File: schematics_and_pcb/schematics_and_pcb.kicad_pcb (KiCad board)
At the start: 2 copper layers, 51.1 x 89.8 mm, 68 parts, among them J1 RND 205-00624, J2 RND 205-00627, J3 Motor con, J4 Conn_01x04_Male, J5 Conn_01x04_Male, J6 USB_OTG_custom, Q1 TSM2308CX RFG, SW1 RND 210-00210, SW2 SW_Push, U1 LP2985IM5-2.0/NOPB, U2 TS3480CX33 RFG, U3 PWM3389DM-T3QU, U4 STM32F401RBTx, U5 LFXTAL055951

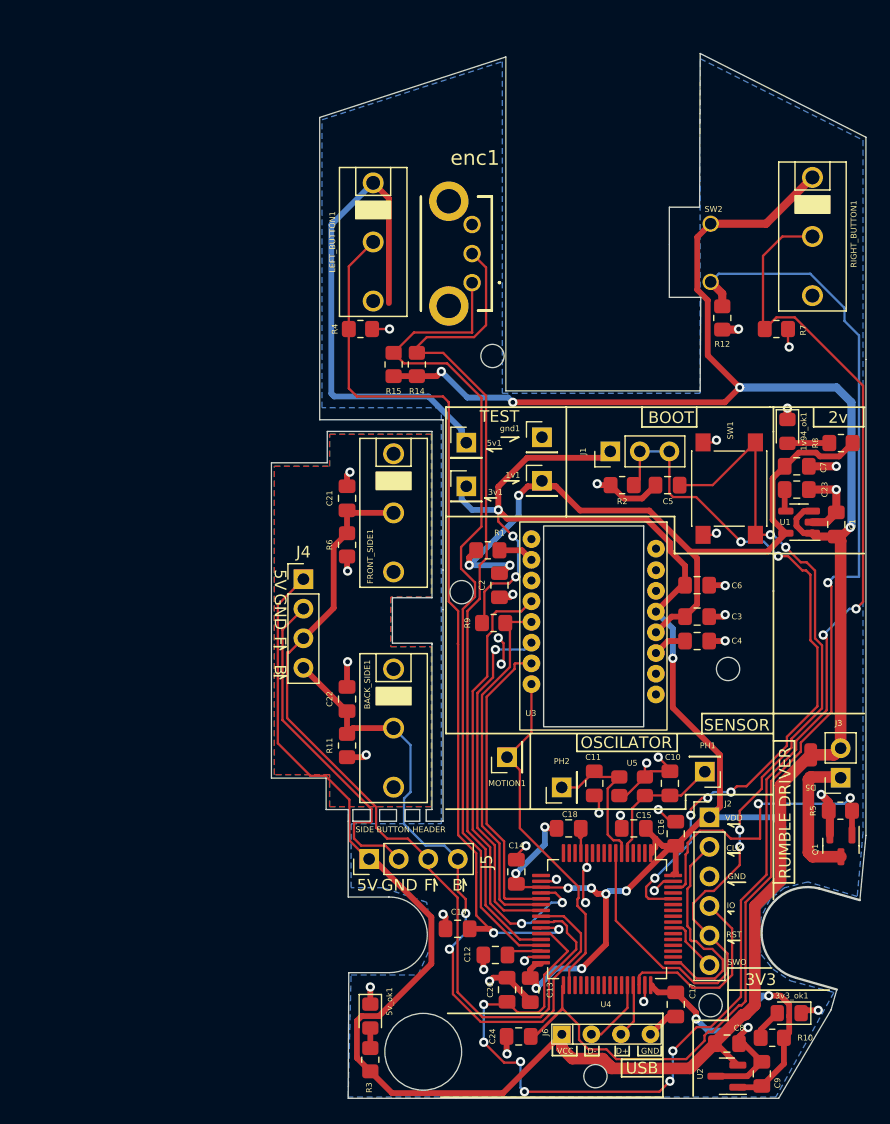
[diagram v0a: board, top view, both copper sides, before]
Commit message: added RGB LEDS
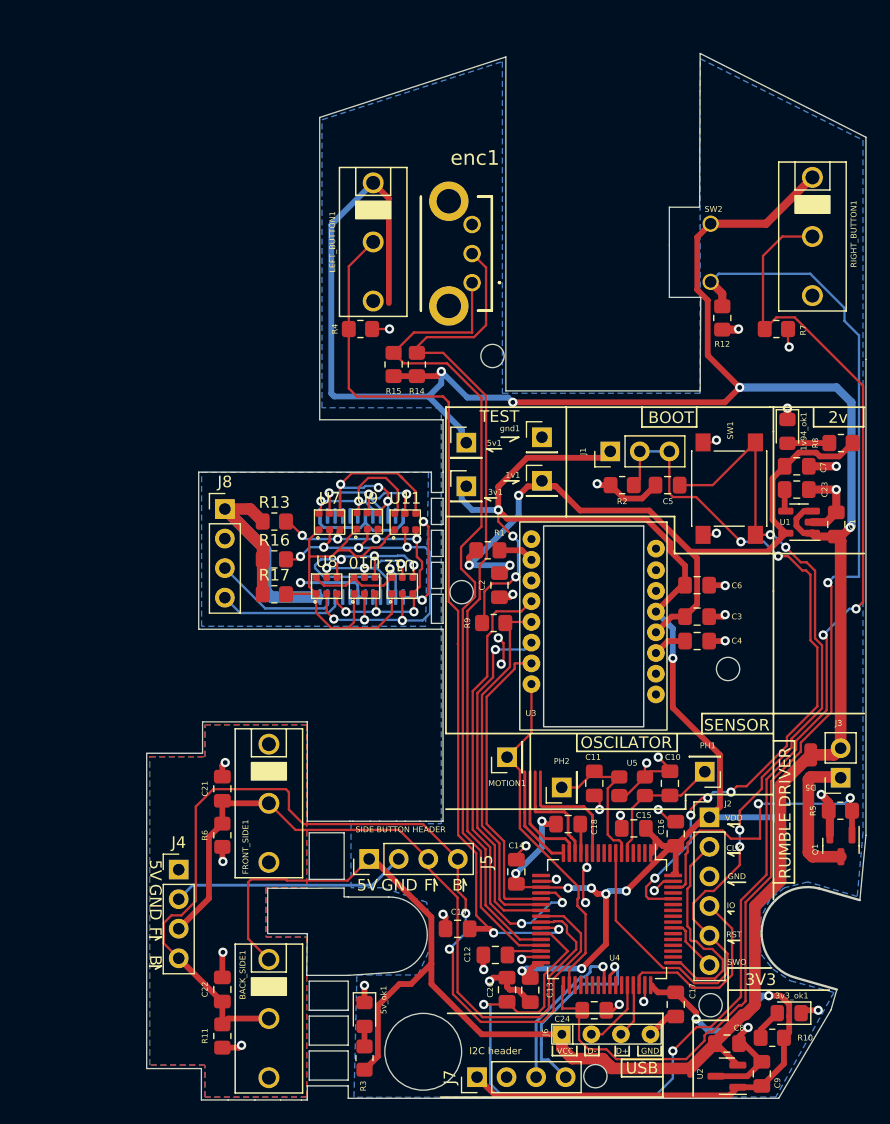
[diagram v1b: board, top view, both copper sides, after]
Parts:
- added J7: i2c header, Connector_PinHeader_2.54mm:PinHeader_1x04_P2.54mm_Vertical, F.Cu at (96.9, 112.5)
- added J8: i2c header, Connector_PinHeader_2.54mm:PinHeader_1x04_P2.54mm_Vertical, F.Cu at (75.2, 63.7)
- added R13: 680m, Resistor_SMD:R_0805_2012Metric_Pad1.20x1.40mm_HandSolder, F.Cu at (79.5, 64.8)
- added R16: 680m, Resistor_SMD:R_0805_2012Metric_Pad1.20x1.40mm_HandSolder, F.Cu at (79.5, 68.0)
- added R17: 8.2, Resistor_SMD:R_0805_2012Metric_Pad1.20x1.40mm_HandSolder, F.Cu at (79.5, 71.0)
- added U10: RND 135-00249, mouse:RND_135-00249, F.Cu at (87.2, 70.2)
- added U11: RND 135-00249, mouse:RND_135-00249, F.Cu at (90.8, 64.8)
- added U12: RND 135-00249, mouse:RND_135-00249, F.Cu at (90.5, 70.2)
- added U6: 9DB403DGLFT, mouse:TSSOP-24, B.Cu at (83.4, 64.3)
- added U7: RND 135-00249, mouse:RND_135-00249, F.Cu at (84.2, 64.8)
- added U8: RND 135-00249, mouse:RND_135-00249, F.Cu at (84.0, 70.2)
- added U9: RND 135-00249, mouse:RND_135-00249, F.Cu at (87.5, 64.7)
- moved BACK_SIDE1 27.2 mm to (79.0, 107.5)
- moved C21 27.2 mm to (75.0, 87.7)
- moved C22 27.2 mm to (75.0, 105.0)
- moved FRONT_SIDE1 27.2 mm to (79.0, 89.0)
- moved R11 27.2 mm to (75.0, 109.0)
- moved R6 27.2 mm to (75.0, 91.7)
- moved J4 27.2 mm to (71.3, 94.7)
- moved C24 6.88 mm to (107.0, 106.8), turned to 180 degrees
- moved 5v_ok1 0.52 mm to (87.2, 107.1)
- moved R3 0.52 mm to (87.2, 110.9)
- moved C18 0.37 mm to (104.8, 90.8)
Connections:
- U4 pad 40: MCO2 -> SDA
- U4 pad 41: MCO1 -> SCL
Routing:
- net VDDIO: track 171.5 -> 222.6 mm
- net VDDG: track 0.00 -> 39.0 mm, vias 0 -> 7
- net VDDR: track 0.00 -> 34.2 mm
- net VDDB: track 0.00 -> 30.6 mm, vias 0 -> 7
- net SCL: track 0.00 -> 28.4 mm, vias 0 -> 1
- net BACK_STATE: track 60.7 -> 87.5 mm
- net SDA: track 0.00 -> 25.4 mm, vias 0 -> 1
- net PWM6: track 0.00 -> 21.7 mm, vias 0 -> 3
- net PWM2: track 0.00 -> 20.0 mm, vias 0 -> 3
- net GND: track 119.4 -> 135.6 mm, vias 39 -> 42
- net PWM0: track 0.00 -> 14.9 mm, vias 0 -> 2
- net PWM1: track 0.00 -> 14.5 mm, vias 0 -> 3
- net PWM5: track 0.00 -> 13.5 mm, vias 0 -> 3
- net +5V: track 273.2 -> 260.3 mm
- net PWM4: track 0.00 -> 11.7 mm, vias 0 -> 1
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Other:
- board size 51.1 x 89.8 mm -> 61.8 x 89.9 mm
- board text added: "I2C header"
- board text added: "SCL"
- board text added: "SDA"
- board text added: "VDDIO"

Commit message: some patches
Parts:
- moved J8 1.75 mm to (73.5, 63.7)
- moved R13 1.75 mm to (77.8, 64.8)
- moved R16 1.75 mm to (77.8, 68.0)
- moved R17 1.75 mm to (77.8, 71.0)
- moved U10 1.75 mm to (85.5, 70.2)
- moved U11 1.75 mm to (89.0, 64.8)
- moved U12 1.75 mm to (88.8, 70.2)
- moved U6 1.75 mm to (81.7, 64.3)
- moved U7 1.75 mm to (82.5, 64.8)
- moved U8 1.75 mm to (82.2, 70.2)
- moved U9 1.75 mm to (85.8, 64.7)
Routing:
- net BACK_STATE: track 87.5 -> 45.7 mm
- net GND: track 135.6 -> 115.2 mm
- net +5V: track 260.3 -> 241.5 mm
- net FRONT_STATE: track 64.7 -> 49.0 mm
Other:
- outline, holes or cut-outs redrawn

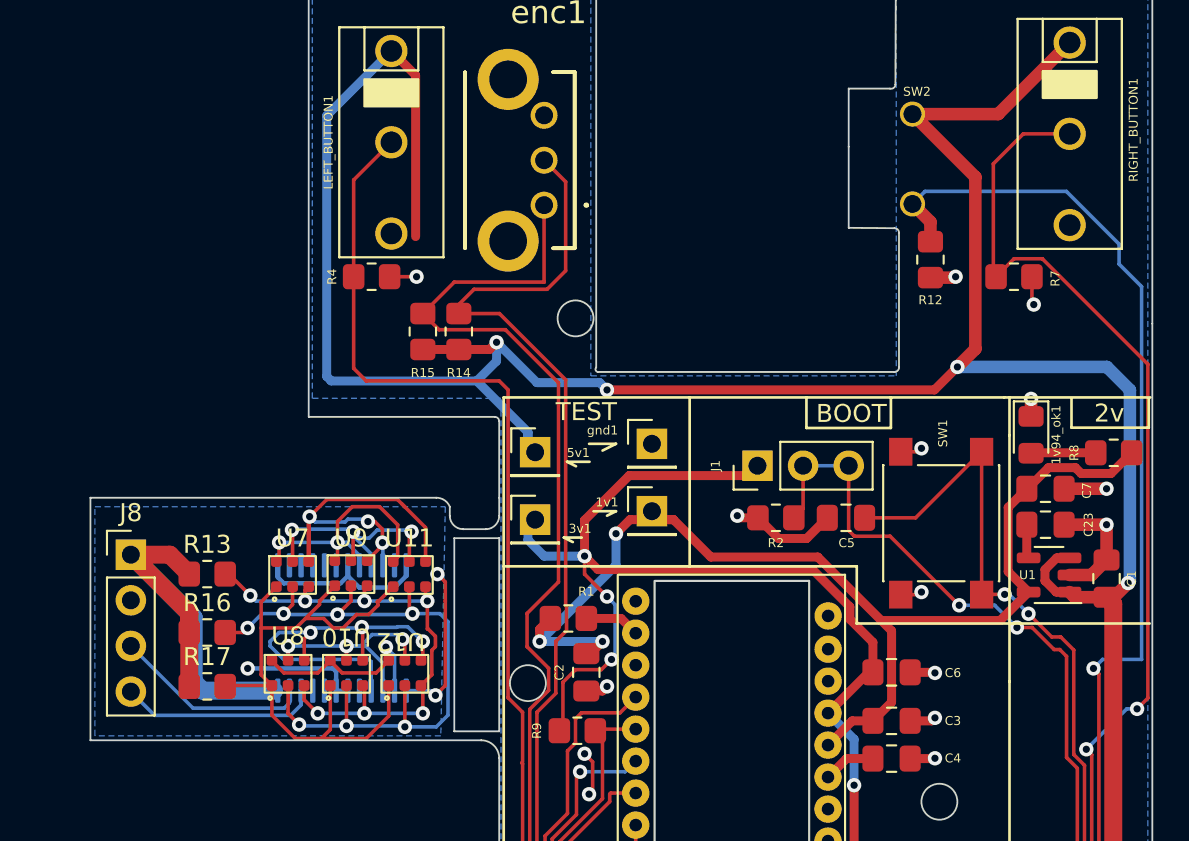
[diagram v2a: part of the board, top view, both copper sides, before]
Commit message: added pullups
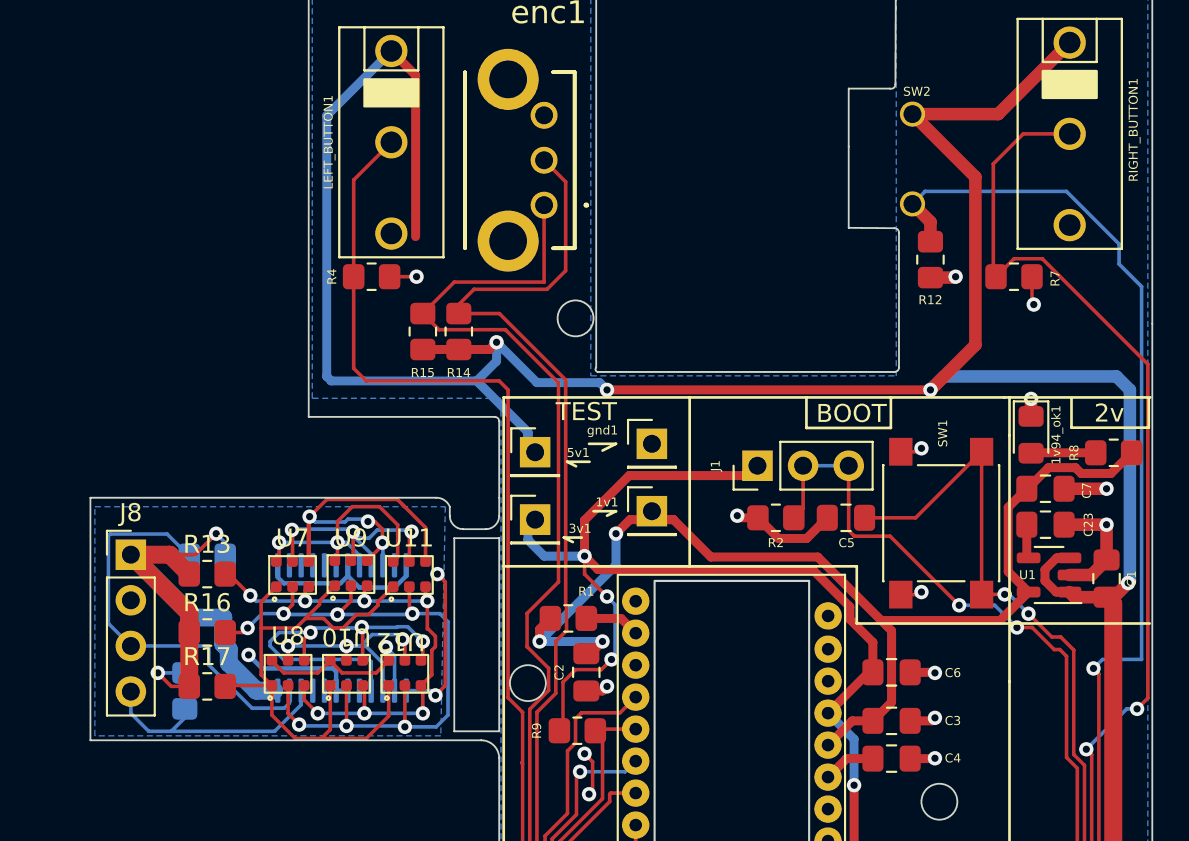
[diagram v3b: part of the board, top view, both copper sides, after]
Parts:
- added R18: 10k, Resistor_SMD:R_0805_2012Metric_Pad1.20x1.40mm_HandSolder, B.Cu at (76.5, 71.2)
- added R19: 10k, Resistor_SMD:R_0805_2012Metric_Pad1.20x1.40mm_HandSolder, B.Cu at (77.8, 63.8)
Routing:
- net SDA: track 25.4 -> 37.7 mm
- net VDDIO: track 222.6 -> 232.1 mm, vias 14 -> 16
- net SCL: track 28.4 -> 31.4 mm
- net +5V: track 241.5 -> 243.0 mm

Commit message: done with the bom
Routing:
- net unconnected-(U4-Pad11): track 11.0 -> 0.00 mm
- net unconnected-(U4-Pad14): track 9.88 -> 0.00 mm
- net unconnected-(U4-Pad15): track 9.42 -> 0.00 mm
- net unconnected-(U4-Pad16): track 8.96 -> 0.00 mm
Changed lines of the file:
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@@
   (gr_line (start 75 66.5) (end 75.75 66.75) (layer "B.SilkS") (width 0.15))
   (gr_line (start 75 64.5) (end 75.75 64.75) (layer "B.SilkS") (width 0.15))
-  (gr_line (start 75 72.25) (end 75.75 72.5) (layer "B.SilkS") (width 0.15))
   (gr_line (start 76.75 69.5) (end 75 69.5) (layer "B.SilkS") (width 0.15))
-  (gr_line (start 77 72.25) (end 75 72.25) (layer "B.SilkS") (width 0.15))
   (gr_line (start 75 69.5) (end 75.75 69.75) (layer "B.SilkS") (width 0.15))
   (gr_line (start 77.75 64.5) (end 75 64.5) (layer "B.SilkS") (width 0.15))
@@
   (gr_line (start 73.2375 112.5) (end 73.2325 114.4625) (layer "Edge.Cuts") (width 0.1))
   (gr_line (start 116.25 53.25) (end 116.25 45.75) (layer "Edge.Cuts") (width 0.1))
-  (gr_arc (start 99.5 53.5) (mid 99.369135 53.407575) (end 99.39808 53.25) (layer "Edge.Cuts") (width 0.1))
+  (gr_arc (start 99.5 53.5) (mid 99.369135 53.407576) (end 99.39808 53.25) (layer "Edge.Cuts") (width 0.1))
   (gr_line (start 83.39808 56) (end 83.39808 30.018068) (layer "Edge.Cuts") (width 0.1))
   (gr_line (start 92 90.5) (end 92.55 90.5) (layer "Edge.Cuts") (width 0.1))
@@
     (effects (font (size 0.75 0.75) (thickness 0.15)) (justify mirror))
   )
-  (gr_text "SCL\n" (at 76 71.5) (layer "B.SilkS")
+  (gr_text "SCL\n" (at 73.5 73.25) (layer "B.SilkS")
     (effects (font (size 0.75 0.75) (thickness 0.15)) (justify mirror))
   )
@@
   (segment (start 101.006148 75.75) (end 101.59808 75.158068) (width 0.2) (layer "B.Cu") (net 25))
   (segment (start 98.5 75.75) (end 101.006148 75.75) (width 0.2) (layer "B.Cu") (net 25))
-  (segment (start 104.45048 89.70048) (end 103.25 89.70048) (width 0.25) (layer "F.Cu") (net 26))
-  (segment (start 105.34808 93.243068) (end 105.34808 92.212363) (width 0.25) (layer "F.Cu") (net 26))
-  (segment (start 105.034277 91.89856) (end 104.75 91.614283) (width 0.25) (layer "F.Cu") (net 26))
-  (segment (start 101.92404 89.67404) (end 101.92404 89.25) (width 0.25) (layer "F.Cu") (net 26))
-  (segment (start 105.34808 92.212363) (end 105.034277 91.89856) (width 0.25) (layer "F.Cu") (net 26))
-  (segment (start 104.75 91.614283) (end 104.75 90) (width 0.25) (layer "F.Cu") (net 26))
-  (segment (start 101.92404 89.25) (end 101.92404 86.25) (width 0.25) (layer "F.Cu") (net 26))
-  (segment (start 104.75 90) (end 104.45048 89.70048) (width 0.25) (layer "F.Cu") (net 26))
-  (segment (start 103.25 89.70048) (end 101.95048 89.70048) (width 0.25) (layer "F.Cu") (net 26))
-  (segment (start 101.95048 89.70048) (end 101.92404 89.67404) (width 0.25) (layer "F.Cu") (net 26))
   (segment (start 100.14952 76.993554) (end 100.149519 77.415487) (width 0.2) (layer "F.Cu") (net 27))
   (segment (start 101.59808 76.938068) (end 100.205006 76.938068) (width 0.2) (layer "F.Cu") (net 27))
@@
   (segment (start 105.84808 90.81058) (end 105.7875 90.75) (width 0.25) (layer "F.Cu") (net 56))
   (segment (start 105.84808 93.243068) (end 105.84808 90.81058) (width 0.25) (layer "F.Cu") (net 56))
-  (segment (start 106.09808 89.25) (end 102.5 89.25) (width 0.25) (layer "F.Cu") (net 64))
-  (segment (start 102.5 89.25) (end 102.37356 89.12356) (width 0.25) (layer "F.Cu") (net 64))
-  (segment (start 102.37356 89.12356) (end 102.37356 86.25) (width 0.25) (layer "F.Cu") (net 64))
-  (segment (start 106.84808 90) (end 106.09808 89.25) (width 0.25) (layer "F.Cu") (net 64))
-  (segment (start 106.84808 93.243068) (end 106.84808 90) (width 0.25) (layer "F.Cu") (net 64))
-  (segment (start 101.47452 90.73844) (end 101.47452 86.25) (width 0.25) (layer "F.Cu") (net 65))
-  (segment (start 104.84808 92.34808) (end 104.5 92) (width 0.25) (layer "F.Cu") (net 65))
-  (segment (start 104.5 92) (end 102.73608 92) (width 0.25) (layer "F.Cu") (net 65))
-  (segment (start 104.84808 93.243068) (end 104.84808 92.34808) (width 0.25) (layer "F.Cu") (net 65))
-  (segment (start 102.73608 92) (end 101.47452 90.73844) (width 0.25) (layer "F.Cu") (net 65))
-  (segment (start 102.100362 92) (end 101.025 90.924638) (width 0.25) (layer "F.Cu") (net 66))
-  (segment (start 101.025 90.924638) (end 101.025 89.75) (width 0.25) (layer "F.Cu") (net 66))
-  (segment (start 103.34343 93.243068) (end 102.100362 92) (width 0.25) (layer "F.Cu") (net 66))
-  (segment (start 101.025 89.75) (end 101.025 86.25) (width 0.25) (layer "F.Cu") (net 66))
-  (segment (start 104.34808 93.243068) (end 103.34343 93.243068) (width 0.25) (layer "F.Cu") (net 66))
   (segment (start 106.5 110.107968) (end 108.046768 110.107968) (width 0.2) (layer "F.Cu") (net 68))
   (segment (start 122.20048 87.068828) (end 124.75048 84.518828) (width 0.2) (layer "F.Cu") (net 68))

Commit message: updated the bom
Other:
- outline, holes or cut-outs redrawn
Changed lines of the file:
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@@
   (gr_line (start 118.49808 105.018068) (end 118.49808 107.618068) (layer "F.SilkS") (width 0.15))
   (gr_line (start 113.45 40.961932) (end 113.45 45.48) (layer "Edge.Cuts") (width 0.1))
-  (gr_line (start 90.75 90.5) (end 92 90.5) (layer "Edge.Cuts") (width 0.1))
   (gr_line (start 113.45 37.73) (end 113.45 40.961932) (layer "Edge.Cuts") (width 0.1))
-  (gr_line (start 86 90.5) (end 86.25 90.5) (layer "Edge.Cuts") (width 0.1))
   (gr_line (start 127.84808 104.968068) (end 124.34808 103.968068) (layer "Edge.Cuts") (width 0.2))
   (gr_arc (start 84.75 96.25) (mid 85.375 96.458333) (end 85.75 97) (layer "Edge.Cuts") (width 0.1))
   (gr_arc (start 80.25 100.1625) (mid 79.256047 99.768909) (end 78.9325 98.75) (layer "Edge.Cuts") (width 0.1))
-  (gr_line (start 83.5 90.5) (end 86 90.5) (layer "Edge.Cuts") (width 0.1))
-  (gr_line (start 88.55 90.5) (end 90 90.5) (layer "Edge.Cuts") (width 0.1))
+  (gr_line (start 83.75 90.7) (end 86.25 90.7) (layer "Edge.Cuts") (width 0.1))
   (gr_arc (start 90.5 60.5) (mid 90.950694 60.636459) (end 91.25 61) (layer "Edge.Cuts") (width 0.1))
   (gr_line (start 85.84808 103.75) (end 83 103.75) (layer "Edge.Cuts") (width 0.1))
@@
   (gr_line (start 122.84808 114.318068) (end 127.34808 106.718068) (layer "Edge.Cuts") (width 0.1))
   (gr_line (start 82.3325 114.4625) (end 81.8325 114.4625) (layer "Edge.Cuts") (width 0.1))
-  (gr_arc (start 93.75 56) (mid 93.926777 56.073223) (end 94 56.25) (layer "Edge.Cuts") (width 0.1))
+  (gr_arc (start 93.75 55.75) (mid 93.934017 55.970491) (end 94 56.25) (layer "Edge.Cuts") (width 0.1))
   (gr_line (start 99.39808 24.818068) (end 83.39808 30.018068) (layer "Edge.Cuts") (width 0.1))
   (gr_line (start 95.14808 114.318068) (end 122.84808 114.318068) (layer "Edge.Cuts") (width 0.1))
@@
   (gr_line (start 116.25 53.25) (end 116.25 45.75) (layer "Edge.Cuts") (width 0.1))
   (gr_arc (start 99.5 53.5) (mid 99.369135 53.407576) (end 99.39808 53.25) (layer "Edge.Cuts") (width 0.1))
-  (gr_line (start 83.39808 56) (end 83.39808 30.018068) (layer "Edge.Cuts") (width 0.1))
-  (gr_line (start 92 90.5) (end 92.55 90.5) (layer "Edge.Cuts") (width 0.1))
+  (gr_line (start 83.39808 55.75) (end 83.39808 30.018068) (layer "Edge.Cuts") (width 0.1))
   (gr_line (start 116.1 24.518068) (end 130.34808 31.718068) (layer "Edge.Cuts") (width 0.1))
   (gr_line (start 94 89.5) (end 94 75) (layer "Edge.Cuts") (width 0.1))
-  (gr_line (start 86.25 90.5) (end 87.75 90.5) (layer "Edge.Cuts") (width 0.1))
+  (gr_line (start 86.25 90.7) (end 87.75 90.7) (layer "Edge.Cuts") (width 0.1))
   (gr_line (start 82.3325 114.318068) (end 82.3325 113.5) (layer "Edge.Cuts") (width 0.1))
   (gr_circle (center 116.995316 106.318068) (end 117.995316 106.318068) (layer "Edge.Cuts") (width 0.1) (fill none))
   (gr_line (start 82.3325 89.25) (end 82.3325 81.9625) (layer "Edge.Cuts") (width 0.1))
   (gr_circle (center 107.09808 112.418068) (end 108.09808 112.418068) (layer "Edge.Cuts") (width 0.1) (fill none))
-  (gr_arc (start 94 89.5) (mid 93.707107 90.207107) (end 93 90.5) (layer "Edge.Cuts") (width 0.1))
+  (gr_arc (start 94 89.5) (mid 93.630731 90.366386) (end 92.75 90.7) (layer "Edge.Cuts") (width 0.1))
   (gr_arc (start 116 45.5) (mid 116.176777 45.573223) (end 116.25 45.75) (layer "Edge.Cuts") (width 0.1))
   (gr_line (start 80.0325 114.4625) (end 77.8325 114.4625) (layer "Edge.Cuts") (width 0.1))
@@
   (gr_line (start 115.75 37.73) (end 113.45 37.73) (layer "Edge.Cuts") (width 0.1))
   (gr_line (start 99.39808 24.818068) (end 99.39808 53.25) (layer "Edge.Cuts") (width 0.1))
-  (gr_line (start 93 90.5) (end 92.55 90.5) (layer "Edge.Cuts") (width 0.1))
   (gr_line (start 82.3325 81.9625) (end 73.3325 81.9625) (layer "Edge.Cuts") (width 0.1))
   (gr_rect (start 85.84808 112.75) (end 82.5 104.25) (layer "Edge.Cuts") (width 0.1) (fill none))
@@
   (gr_arc (start 116.25 53.25) (mid 116.176777 53.426777) (end 116 53.5) (layer "Edge.Cuts") (width 0.1))
   (gr_line (start 68.5325 84.6625) (end 68.5325 111.7625) (layer "Edge.Cuts") (width 0.1))
-  (gr_line (start 87.75 90.5) (end 88.55 90.5) (layer "Edge.Cuts") (width 0.1))
   (gr_line (start 93.25 62.25) (end 92 62.25) (layer "Edge.Cuts") (width 0.1))
   (gr_line (start 91.25 61) (end 91.25 61.5) (layer "Edge.Cuts") (width 0.1))
+  (gr_line (start 87.75 90.7) (end 92.75 90.7) (layer "Edge.Cuts") (width 0.1))
   (gr_line (start 130.34808 50.818068) (end 130.34808 91.718068) (layer "Edge.Cuts") (width 0.1))
   (gr_line (start 85.5 113.25) (end 82.5 113.25) (layer "Edge.Cuts") (width 0.1))
@@
   (gr_line (start 78.9325 98.75) (end 78.9325 97.75) (layer "Edge.Cuts") (width 0.1))
   (gr_line (start 129.82808 97.288068) (end 130.34808 91.718068) (layer "Edge.Cuts") (width 0.1))
-  (gr_arc (start 83.5 90.5) (mid 82.644787 90.128546) (end 82.3325 89.25) (layer "Edge.Cuts") (width 0.1))
+  (gr_arc (start 83.75 90.7) (mid 82.716488 90.292482) (end 82.3325 89.25) (layer "Edge.Cuts") (width 0.1))
   (gr_line (start 80.5 96.259835) (end 82.3325 96.2625) (layer "Edge.Cuts") (width 0.1))
   (gr_line (start 99.5 53.5) (end 116 53.5) (layer "Edge.Cuts") (width 0.1))
@@
   (gr_line (start 80.0325 114.4625) (end 81.8325 114.4625) (layer "Edge.Cuts") (width 0.1))
   (gr_line (start 85.75 97) (end 89.34808 97.018068) (layer "Edge.Cuts") (width 0.1))
-  (gr_line (start 83.39808 56) (end 93.75 56) (layer "Edge.Cuts") (width 0.1))
+  (gr_line (start 83.39808 55.75) (end 93.75 55.75) (layer "Edge.Cuts") (width 0.1))
   (gr_line (start 71.25 60.5) (end 71.25 74) (layer "Edge.Cuts") (width 0.1))
   (gr_arc (start 83 103.75) (mid 82.49799 103.524751) (end 82.3325 103) (layer "Edge.Cuts") (width 0.1))
@@
   (gr_arc (start 78.9325 97.75) (mid 79.437437 96.711635) (end 80.5 96.259835) (layer "Edge.Cuts") (width 0.1))
   (gr_circle (center 92.29808 110.318068) (end 95.59808 110.318068) (layer "Edge.Cuts") (width 0.1) (fill none))
-  (gr_line (start 90 90.5) (end 90.75 90.5) (layer "Edge.Cuts") (width 0.1))
   (gr_text "SDA\n" (at 76 69) (layer "B.SilkS")
     (effects (font (size 0.75 0.75) (thickness 0.15)) (justify mirror))
